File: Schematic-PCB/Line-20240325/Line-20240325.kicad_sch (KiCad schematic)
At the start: 167 parts, among them J1 Conn_01x02_Pin, J2 Conn_01x04_Pin, J3 Conn_01x06_Pin, J4 ICSP, Q1 NMOS 60V-5V, SW1 SW_Push, SW2 SW_DPST_x2, U33 ATmega2560-16A, Y1 16MHz

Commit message: update: ラインセンサ基板の回路をモジュール使用のものに更新
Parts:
- removed C10: LPF, Capacitor_SMD:C_0603_1608Metric, symbol Device:C_Small
- removed C5, C8: 0.1uF, Capacitor_SMD:C_0603_1608Metric, symbol Device:C_Small
- removed C6, C7, C9: 22pF, Capacitor_SMD:C_0603_1608Metric, symbol Device:C_Small
- removed D34: LED3, LED_SMD:LED_0805_2012Metric, symbol Device:LED_Small_Filled
- removed D35: LED2, LED_SMD:LED_0805_2012Metric, symbol Device:LED_Small_Filled
- removed D36: LED1, LED_SMD:LED_0805_2012Metric, symbol Device:LED_Small_Filled
- removed J3: Conn_01x06_Pin, Connector_PinSocket_2.54mm:PinSocket_1x06_P2.54mm_Horizontal, symbol Connector:Conn_01x06_Pin
- removed J4: ICSP, symbol Connector_Generic:Conn_02x03_Odd_Even
- removed R66: 1M, Resistor_SMD:R_0603_1608Metric, symbol Device:R_Small
- removed R67, R69, R70: 330, Resistor_SMD:R_0603_1608Metric, symbol Device:R_Small
- removed R71: 10K, Resistor_SMD:R_0603_1608Metric, symbol Device:R_Small
- removed R72: LPF, Resistor_SMD:R_0603_1608Metric, symbol Device:R_Small
- removed SW1: SW_Push, @2024TOINIOT2-Line:Tactile1, symbol Switch:SW_Push
- removed U33: ATmega2560-16A, Package_QFP:TQFP-100_14x14mm_P0.5mm, symbol @2024TOINIOT2-Line:ATmega2560-16A
- removed Y1: 16MHz, @2024TOINIOT2-Line:AL4BT, symbol Device:Crystal
- added Comp10, Comp9: ~, @2024TOINIOT2-Line:LM339, symbol @2024-Line:LM339
- added D37, D38, D39, D40, D41: LED_Small, @2024TOINIOT2-Line:LED-3mm, symbol Device:LED_Small
- added R73, R74, R75, R76, R77: Line-Pulldown, Resistor_SMD:R_0603_1608Metric, symbol Device:R_Small
- added R78, R79, R80, R81, R82: 75, Resistor_SMD:R_0603_1608Metric, symbol Device:R_Small
- added U33: ATMEGA2560_pro, @2023_MainBoard:MODULE_MEGA_PRO_EMBED_CH340G___ATMEGA2560, symbol @2023_MainBoard:ATMEGA2560_pro
- added U34, U35, U36, U37, U38: ~, @2024TOINIOT2-Line:NJL7502L, symbol @2024TOINIOT2-Line:NJL7502L
- J2: value Conn_01x04_Pin -> Conn_MD
- Q1: value NMOS 60V-5V -> NMOS 60V-5A
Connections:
- net +5V: now also Comp10.3 (VCC), Comp9.3 (VCC), U33.5V_1 (5V), U33.5V_2 (5V), U33.5V_3 (5V), U33.VIN_1 (VIN), U33.VIN_2 (VIN), U34.2 (Collector), U35.2 (Collector), U36.2 (Collector), U37.2 (Collector), U38.2 (Collector)
- net GND: now also Comp10.12 (GND), Comp9.12 (GND), D37.1 (K), D38.1 (K), D39.1 (K), D40.1 (K), D41.1 (K), R73.2, R74.2, R75.2, R76.2, R77.2, U33.GND_1 (GND), U33.GND_2 (GND), U33.GND_3 (GND)
- net LED_5V: now also R78.2, R79.2, R80.2, R81.2, R82.2
- net Line01: now also U33.D2
- net Line02: now also U33.D3
- net Line03: now also U33.D4
- net Line04: now also U33.D5
- net Line05: now also U33.D6
- net Line06: now also U33.D7
- net Line07: now also U33.D8
- net Line08: now also U33.D9
- net Line13: now also U33.D14
- net Line14: now also U33.D15
- net Line15: now also U33.D16
- net Line16: now also U33.D17
- net Line17: now also U33.D18
- net Line18: now also U33.D19
- net Line19: now also U33.D20
- net Line20: now also U33.D21
- net Line21: now also U33.D22
- net Line22: now also U33.D23
- net Line23: now also U33.D24
- net Line24: now also U33.D25
- net Line25: now also U33.D26
- net Line26: now also U33.D27
- net Line27: now also U33.D28
- net Line28: now also U33.D29
- net Line29: now also U33.D30
- net Line30: now also U33.D31
- net Line31: now also U33.D32
- net Line32: now also U33.D33
- net LineThreshold: now also Comp10.6 (1IN-), Comp9.10 (4IN-), Comp9.4 (2IN-), Comp9.6 (1IN-), Comp9.8 (3IN-)
- net Line-MD-Main=RX_5V renamed Line-Main=RX_5V
- net Line-MD-Main=TX_5V renamed Line-Main=TX_5V
- net Line09_SS renamed Line09
- net Line09: now also U33.D10
- net Line10_SCK renamed Line10
- net Line10: now also U33.D11
- net Line11MOSI renamed Line11
- net Line11: now also U33.D12
- net Line12_MISO renamed Line12
- net Line12: now also U33.D13
- new net: D38.2 (A), R79.1
- new net: D37.2 (A), R78.1
- new net: D41.2 (A), R82.1
- new net: D40.2 (A), R81.1
- new net: U33.3V3_1 (3V3), U33.3V3_2 (3V3)
- new net: D39.2 (A), R80.1
- new net Line33: Comp9.1 (1OUT), U33.D34
- new net Line34: Comp9.2 (2OUT), U33.D35
- new net Line35: Comp9.14 (3OUT), U33.D36
- new net Line36: Comp9.13 (4OUT), U33.D37
- new net Line37: Comp10.1 (1OUT), U33.D38
- new net Raw33: Comp9.7 (1IN+), R73.1, U34.1 (Emitter)
- new net Raw34: Comp9.5 (2IN+), R74.1, U35.1 (Emitter)
- new net Raw35: Comp9.9 (3IN+), R75.1, U36.1 (Emitter)
- new net Raw36: Comp9.11 (4IN+), R76.1, U37.1 (Emitter)
- new net Raw37: Comp10.7 (1IN+), R77.1, U38.1 (Emitter)
- no-connect marks 40 -> 15
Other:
- note removed: "Comparator"
- note removed: "ICSP"
- note removed: "LED"
- note removed: "MPU"
- note removed: "RESET"
- note removed: "Sensors"
- note removed: "To Motor Driver"
- note removed: "To PC"
- note removed: "クロックの発振子からMPUのピンまでの距離は同距離にする"
- moved on the sheet: C1, C2, C3, C4, Comp1, Comp2, Comp3, Comp4, Comp5, Comp6, Comp7, Comp8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

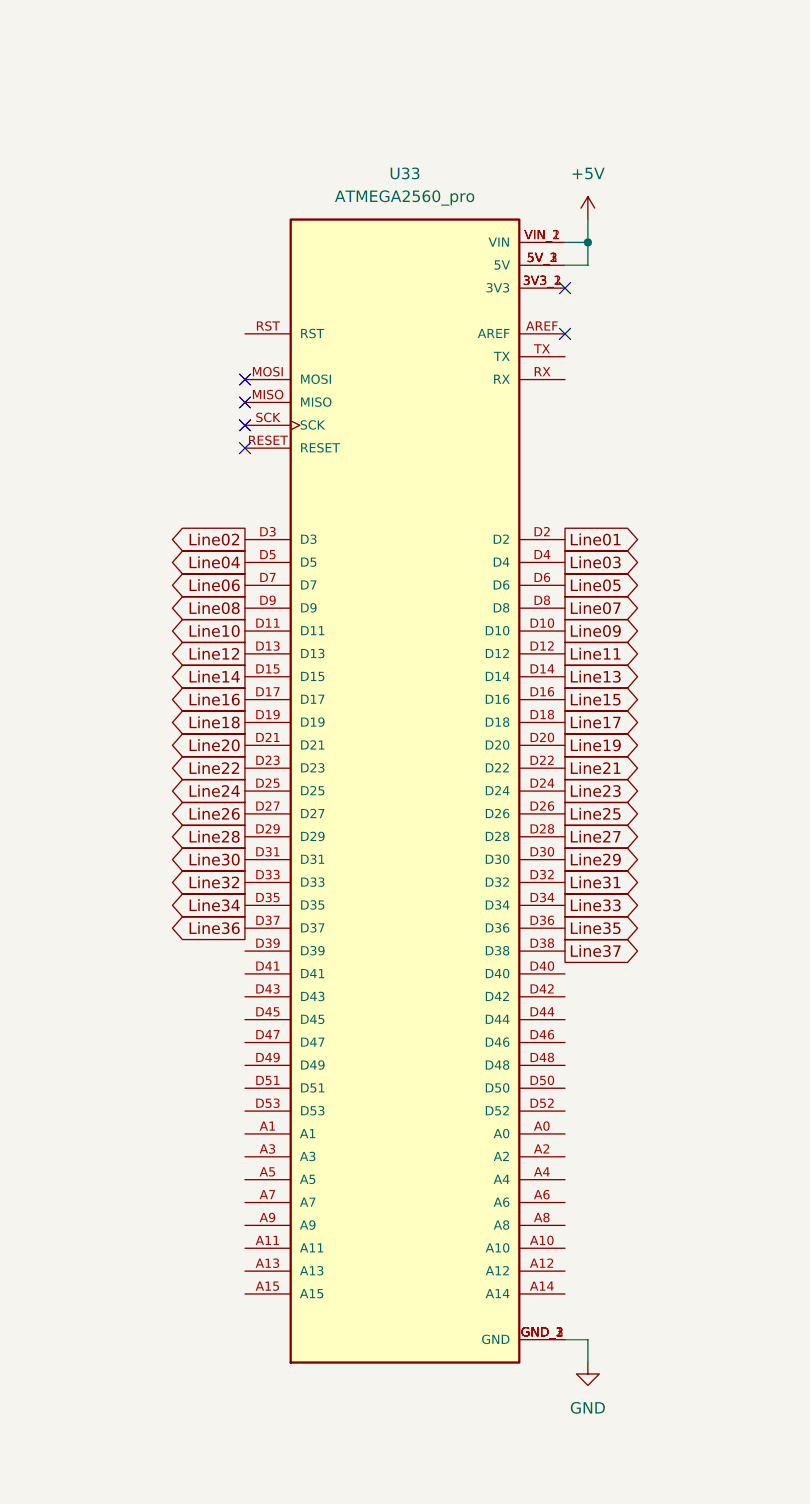
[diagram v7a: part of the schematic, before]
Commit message: update: ラインセンサ基板のKiCadファイルにATmega2560proのボード関連ファイルを追加した
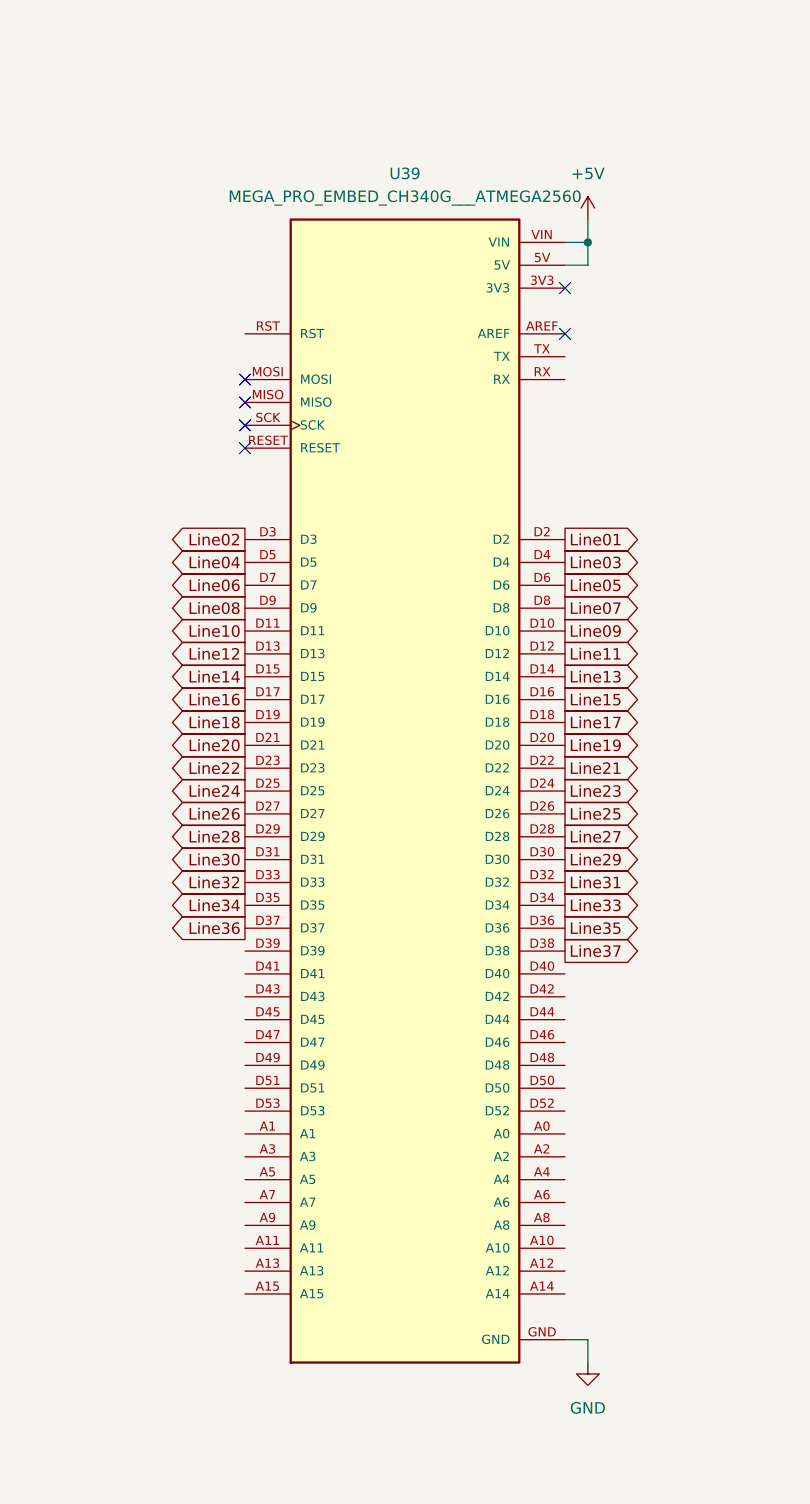
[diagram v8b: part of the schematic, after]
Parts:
- removed U33: ATMEGA2560_pro, @2023_MainBoard:MODULE_MEGA_PRO_EMBED_CH340G___ATMEGA2560, symbol @2023_MainBoard:ATMEGA2560_pro
- added U39: MEGA_PRO_EMBED_CH340G___ATMEGA2560, MEGA_PRO_EMBED_CH340G___ATMEGA2560:MODULE_MEGA_PRO_EMBED_CH340G___ATMEGA2560, symbol @2024-Line:MEGA_PRO_EMBED_CH340G___ATMEGA2560
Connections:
- net +5V: now also U39.5V, U39.VIN
- net GND: now also U39.GND
- net Line01: now also U39.D2
- net Line02: now also U39.D3
- net Line03: now also U39.D4
- net Line04: now also U39.D5
- net Line05: now also U39.D6
- net Line06: now also U39.D7
- net Line07: now also U39.D8
- net Line08: now also U39.D9
- net Line09: now also U39.D10
- net Line10: now also U39.D11
- net Line11: now also U39.D12
- net Line12: now also U39.D13
- net Line13: now also U39.D14
- net Line14: now also U39.D15
- net Line15: now also U39.D16
- net Line16: now also U39.D17
- net Line17: now also U39.D18
- net Line18: now also U39.D19
- net Line19: now also U39.D20
- net Line20: now also U39.D21
- net Line21: now also U39.D22
- net Line22: now also U39.D23
- net Line23: now also U39.D24
- net Line24: now also U39.D25
- net Line25: now also U39.D26
- net Line26: now also U39.D27
- net Line27: now also U39.D28
- net Line28: now also U39.D29
- net Line29: now also U39.D30
- net Line30: now also U39.D31
- net Line31: now also U39.D32
- net Line32: now also U39.D33
- net Line33: now also U39.D34
- net Line34: now also U39.D35
- net Line35: now also U39.D36
- net Line36: now also U39.D37
- net Line37: now also U39.D38
